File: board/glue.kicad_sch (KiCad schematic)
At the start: 2 parts, among them U9 ATF1504AS-xAx44

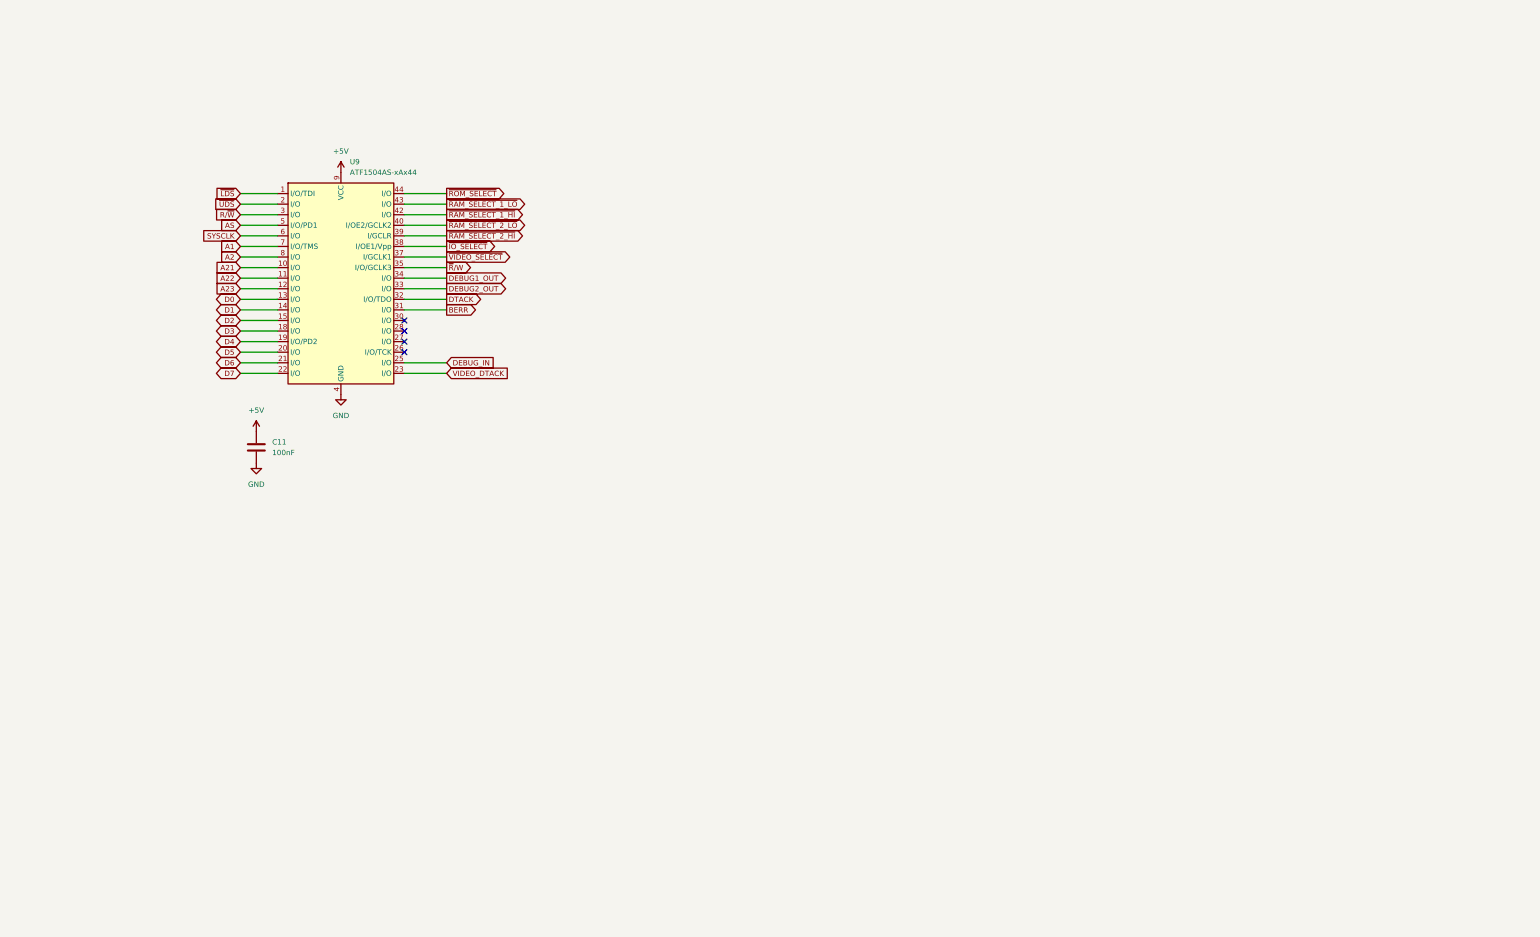
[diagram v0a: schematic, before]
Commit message: fill out most functionality - passes ERC
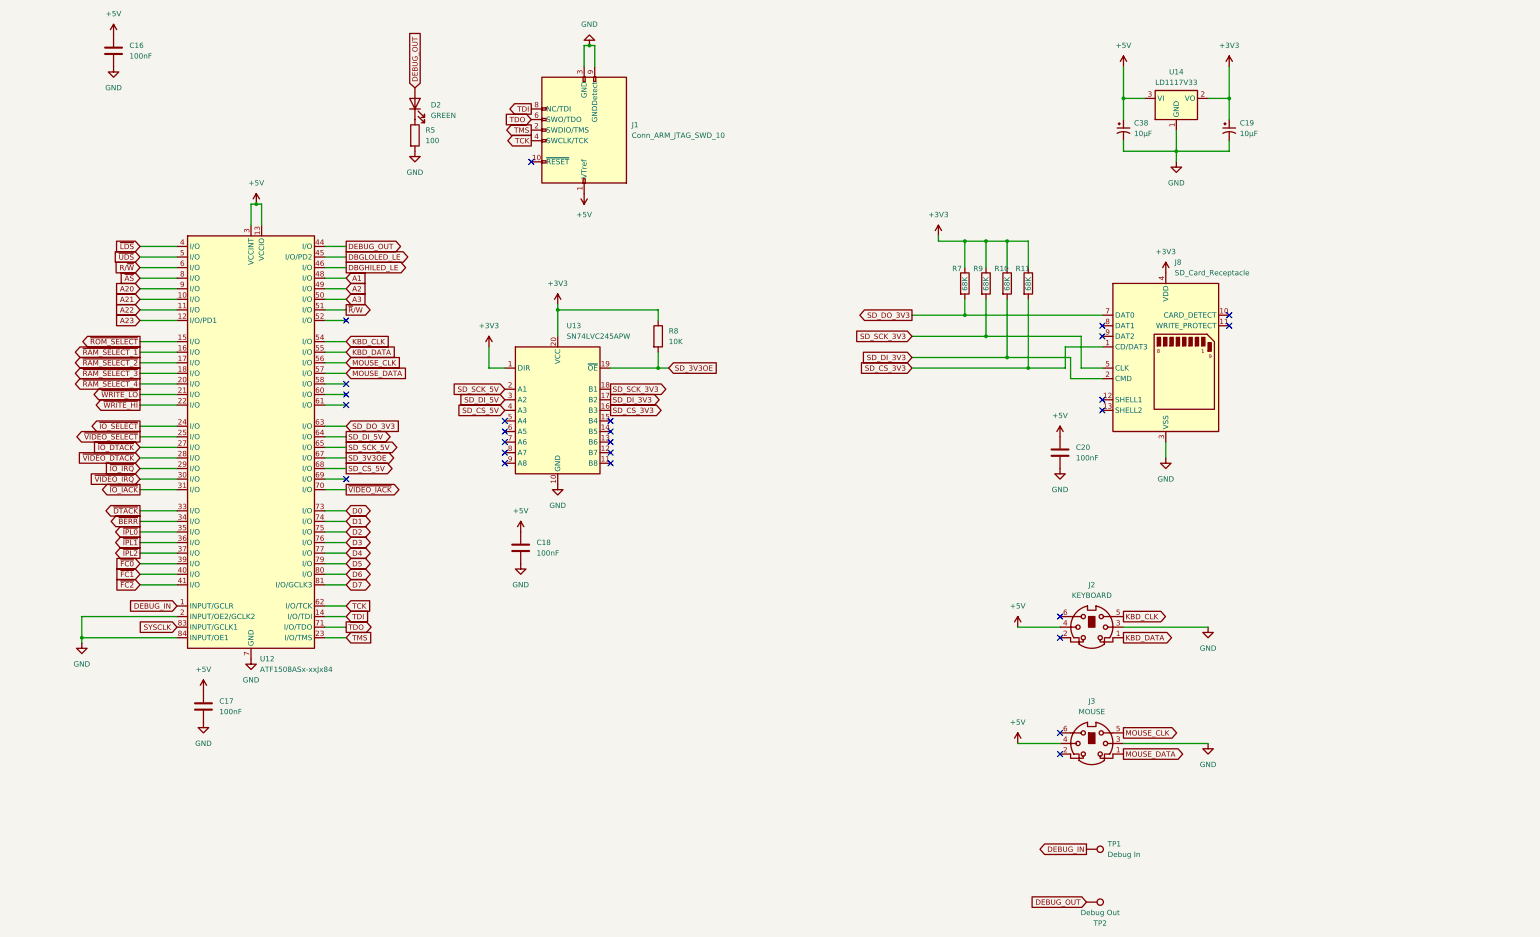
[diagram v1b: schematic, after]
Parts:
- removed U9: ATF1504AS-xAx44, Package_QFP:TQFP-44_10x10mm_P0.8mm, symbol CPLD_Microchip:ATF1504AS-xAx44
- added C16, C18, C20: 100nF, symbol Device:C
- added C19, C38: 10µF, symbol Device:C_Polarized_Small_US
- added D2: GREEN, LED_THT:LED_D3.0mm, symbol Device:LED
- added J1: Conn_ARM_JTAG_SWD_10, symbol Connector:Conn_ARM_JTAG_SWD_10
- added J2: KEYBOARD, symbol Connector:Mini-DIN-6
- added J3: MOUSE, symbol Connector:Mini-DIN-6
- added J8: SD_Card_Receptacle, symbol Connector:SD_Card_Receptacle
- added R10, R11, R7, R9: 68K, symbol Device:R
- added R5: 100, symbol Device:R
- added R8: 10K, symbol Device:R
- added TP1: Debug In, symbol Connector:TestPoint
- added TP2: Debug Out, symbol Connector:TestPoint
- added U12: ATF1508ASx-xxJx84, Package_LCC:PLCC-84_29.3x29.3mm_P1.27mm, symbol CPLD_Microchip:ATF1508ASx-xxJx84
- added U13: SN74LVC245APW, Package_SO:TSSOP-20_4.4x6.5mm_P0.65mm, symbol Logic_LevelTranslator:SN74LVC245APW
- added U14: LD1117V33, Package_TO_SOT_THT:TO-220-3_Vertical, symbol Regulator_Linear:LD1117V33
- renumbered C11 to C17
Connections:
- net +5V: now also C16.1, C18.1, C20.1, C38.1, J1.1 (VTref), J2.4, J3.4, U12.13 (VCCIO), U12.26 (VCCIO), U12.3 (VCCINT), U12.38 (VCCIO), U12.43 (VCCINT), U12.53 (VCCIO), U12.66 (VCCIO), U12.78 (VCCIO), U14.3 (VI)
- net A1: now also U12.48 (I/O)
- net A2: now also U12.49 (I/O)
- net A21: now also U12.10 (I/O)
- net A22: now also U12.11 (I/O)
- net A23: now also U12.12 (I/O/PD1)
- net D0: now also U12.73 (I/O)
- net D1: now also U12.74 (I/O)
- net D2: now also U12.75 (I/O)
- net D3: now also U12.76 (I/O)
- net D4: now also U12.77 (I/O)
- net D5: now also U12.79 (I/O)
- net D6: now also U12.80 (I/O)
- net D7: now also U12.81 (I/O/GCLK3)
- net DEBUG_IN: now also TP1.1, U12.1 (INPUT/GCLR)
- net GND: now also C16.2, C18.2, C19.2, C20.2, C38.2, J1.3 (GND), J1.5 (GND), J1.9 (GNDDetect), J2.3, J3.3, J8.3 (VSS), J8.6 (VSS), R5.2, U12.19 (GND), U12.2 (INPUT/OE2/GCLK2), U12.32 (GND), U12.42 (GND), U12.47 (GND), U12.59 (GND), U12.7 (GND), U12.72 (GND), U12.82 (GND), U12.84 (INPUT/OE1), U13.10 (GND), U14.1 (GND)
- net R/~{W}: now also U12.6 (I/O)
- net SYSCLK: now also U12.83 (INPUT/GCLK1)
- net ~{IO_SELECT}: now also U12.24 (I/O)
- net ~{LDS}: now also U12.4 (I/O)
- net ~{ROM_SELECT}: now also U12.15 (I/O)
- net ~{R}/W: now also U12.51 (I/O)
- net ~{UDS}: now also U12.5 (I/O)
- net ~{VIDEO_SELECT}: now also U12.25 (I/O)
- new net: D2.1 (K), R5.1
- new net +3V3: C19.1, J8.4 (VDD), R10.1, R11.1, R7.1, R8.1, R9.1, U13.1 (DIR), U13.20 (VCC), U14.2 (VO)
- new net A20: U12.9 (I/O)
- new net A3: U12.50 (I/O)
- new net DBGHILED_LE: U12.46 (I/O)
- new net DBGLOLED_LE: U12.45 (I/O/PD2)
- new net DEBUG_OUT: D2.2 (A), TP2.1, U12.44 (I/O)
- new net KBD_CLK: J2.5, U12.54 (I/O)
- new net KBD_DATA: J2.1, U12.55 (I/O)
- new net MOUSE_CLK: J3.5, U12.56 (I/O)
- new net MOUSE_DATA: J3.1, U12.57 (I/O)
- new net SD_3V3OE: R8.2, U12.67 (I/O), U13.19 (~{OE})
- new net SD_CS_3V3: J8.1 (CD/DAT3), R11.2, U13.16 (B3)
- new net SD_CS_5V: U12.68 (I/O), U13.4 (A3)
- new net SD_DI_3V3: J8.2 (CMD), R10.2, U13.17 (B2)
- new net SD_DI_5V: U12.64 (I/O), U13.3 (A2)
- new net SD_DO_3V3: J8.7 (DAT0), R7.2, U12.63 (I/O)
- new net SD_SCK_3V3: J8.5 (CLK), R9.2, U13.18 (B1)
- new net SD_SCK_5V: U12.65 (I/O), U13.2 (A1)
- new net TCK: J1.4 (SWCLK/TCK), U12.62 (I/O/TCK)
- new net TDI: J1.8 (NC/TDI), U12.14 (I/O/TDI)
- new net TDO: J1.6 (SWO/TDO), U12.71 (I/O/TDO)
- new net TMS: J1.2 (SWDIO/TMS), U12.23 (I/O/TMS)
- new net ~{AS}: U12.8 (I/O)
- new net ~{BERR}: U12.34 (I/O)
- new net ~{DTACK}: U12.33 (I/O)
- new net ~{FC0}: U12.39 (I/O)
- new net ~{FC1}: U12.40 (I/O)
- new net ~{FC2}: U12.41 (I/O)
- new net ~{IO_DTACK}: U12.27 (I/O)
- new net ~{IO_IACK}: U12.31 (I/O)
- new net ~{IO_IRQ}: U12.29 (I/O)
- new net ~{IPL0}: U12.35 (I/O)
- new net ~{IPL1}: U12.36 (I/O)
- new net ~{IPL2}: U12.37 (I/O)
- new net ~{RAM_SELECT_1}: U12.16 (I/O)
- new net ~{RAM_SELECT_2}: U12.17 (I/O)
- new net ~{RAM_SELECT_3}: U12.18 (I/O)
- new net ~{RAM_SELECT_4}: U12.20 (I/O)
- new net ~{VIDEO_DTACK}: U12.28 (I/O)
- new net ~{VIDEO_IACK}: U12.70 (I/O)
- new net ~{VIDEO_IRQ}: U12.30 (I/O)
- new net ~{WRITE_HI}: U12.22 (I/O)
- new net ~{WRITE_LO}: U12.21 (I/O)
- no-connect marks 4 -> 26
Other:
- moved on the sheet: C17

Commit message: change IO to 8051 variant, add audio
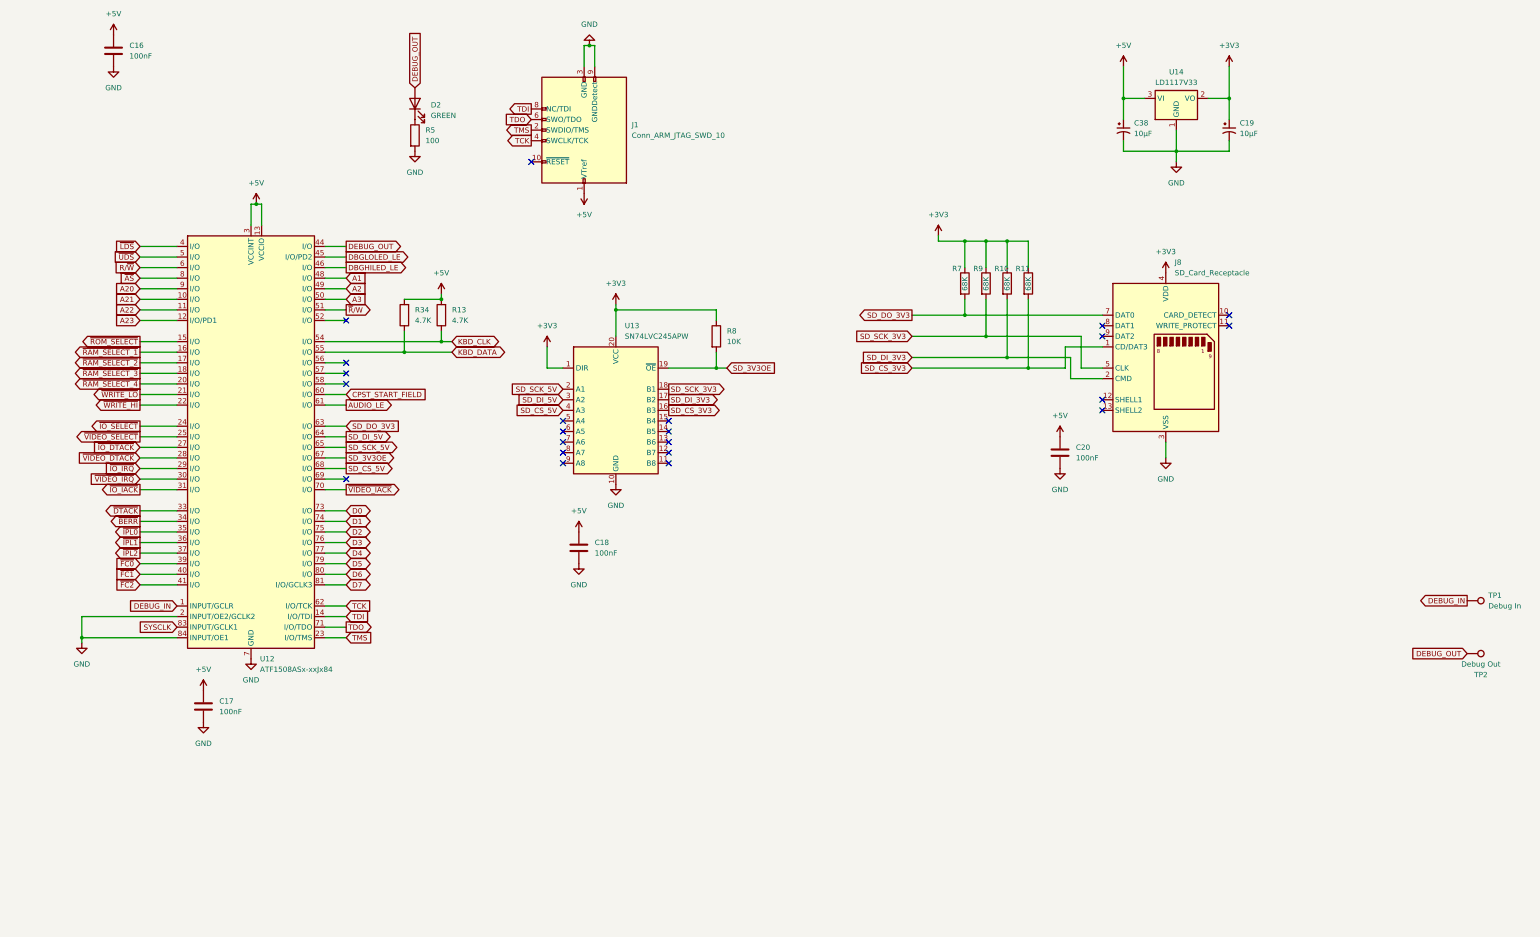
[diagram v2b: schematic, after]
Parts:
- removed J2: KEYBOARD, symbol Connector:Mini-DIN-6
- removed J3: MOUSE, symbol Connector:Mini-DIN-6
- added R13, R34: 4.7K, symbol Device:R
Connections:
- net +5V: now also R13.2, R34.2
- net KBD_CLK: now also R13.1
- net KBD_DATA: now also R34.1
- net CPST_START_FIELD: now reaches U12.60 (I/O)
- net AUDIO_LE: now reaches U12.61 (I/O)
- net MOUSE_CLK: no longer names the net of U12.56 (I/O)
- net MOUSE_DATA: no longer names the net of U12.57 (I/O)
- no-connect marks 26 -> 22
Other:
- moved on the sheet: C18, R8, TP1, TP2, U13

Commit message: design draft complete, added footprints
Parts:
- removed C16: 100nF, symbol Device:C
- removed R13, R34: 4.7K, symbol Device:R
- added R56: 10K, Resistor_THT:R_Axial_DIN0207_L6.3mm_D2.5mm_P10.16mm_Horizontal, symbol Device:R
- C17, C18, C20: footprint (none) -> Capacitor_THT:C_Disc_D5.0mm_W2.5mm_P5.00mm
- C19, C38: footprint (none) -> Capacitor_THT:CP_Radial_D5.0mm_P2.50mm
- J1: footprint (none) -> Connector_PinHeader_1.27mm:PinHeader_2x05_P1.27mm_Vertical
- J8: footprint (none) -> board:10067847-001RLF
- R10, R11, R5, R7, R8, R9: footprint (none) -> Resistor_THT:R_Axial_DIN0207_L6.3mm_D2.5mm_P10.16mm_Horizontal
- TP1, TP2: footprint (none) -> Connector_PinHeader_2.54mm:PinHeader_1x01_P2.54mm_Vertical
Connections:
- net DEBUG_IN: now also R56.1
- net GND: now also R56.2; no longer U12.2 (INPUT/OE2/GCLK2)
- net ~{HALT}: now reaches U12.52 (I/O)
- net KBD_CLK: no longer names the net of U12.54 (I/O)
- net KBD_DATA: no longer names the net of U12.55 (I/O)
- new net ~{RESET}: U12.2 (INPUT/OE2/GCLK2)
- no-connect marks 22 -> 23
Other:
- moved on the sheet: TP1, TP2

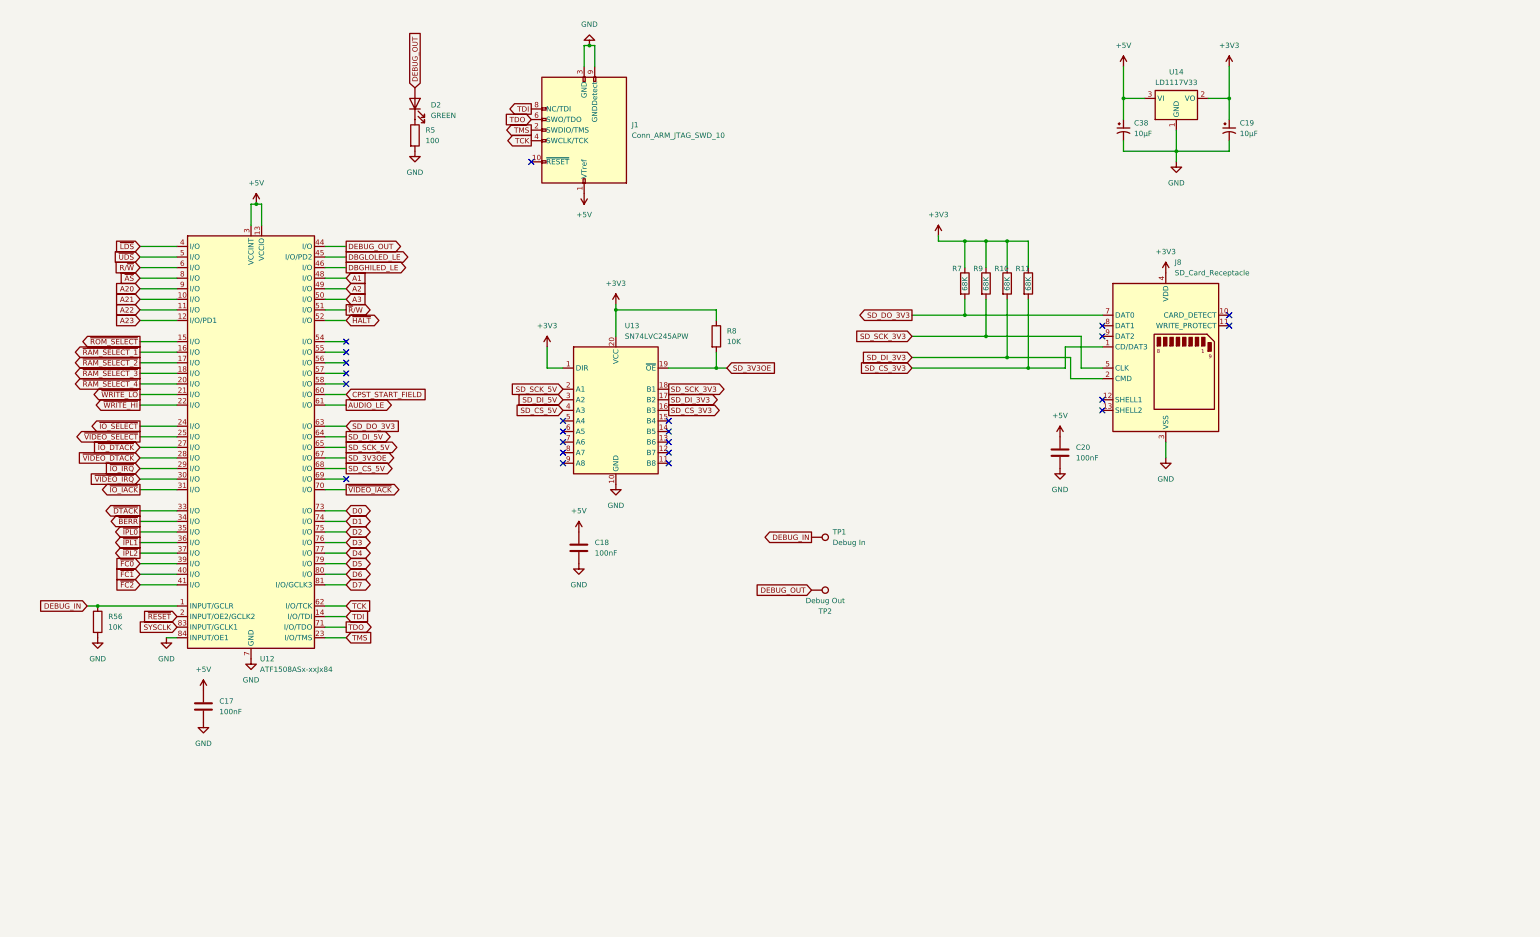
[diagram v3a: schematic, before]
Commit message: start of PCB and MMU
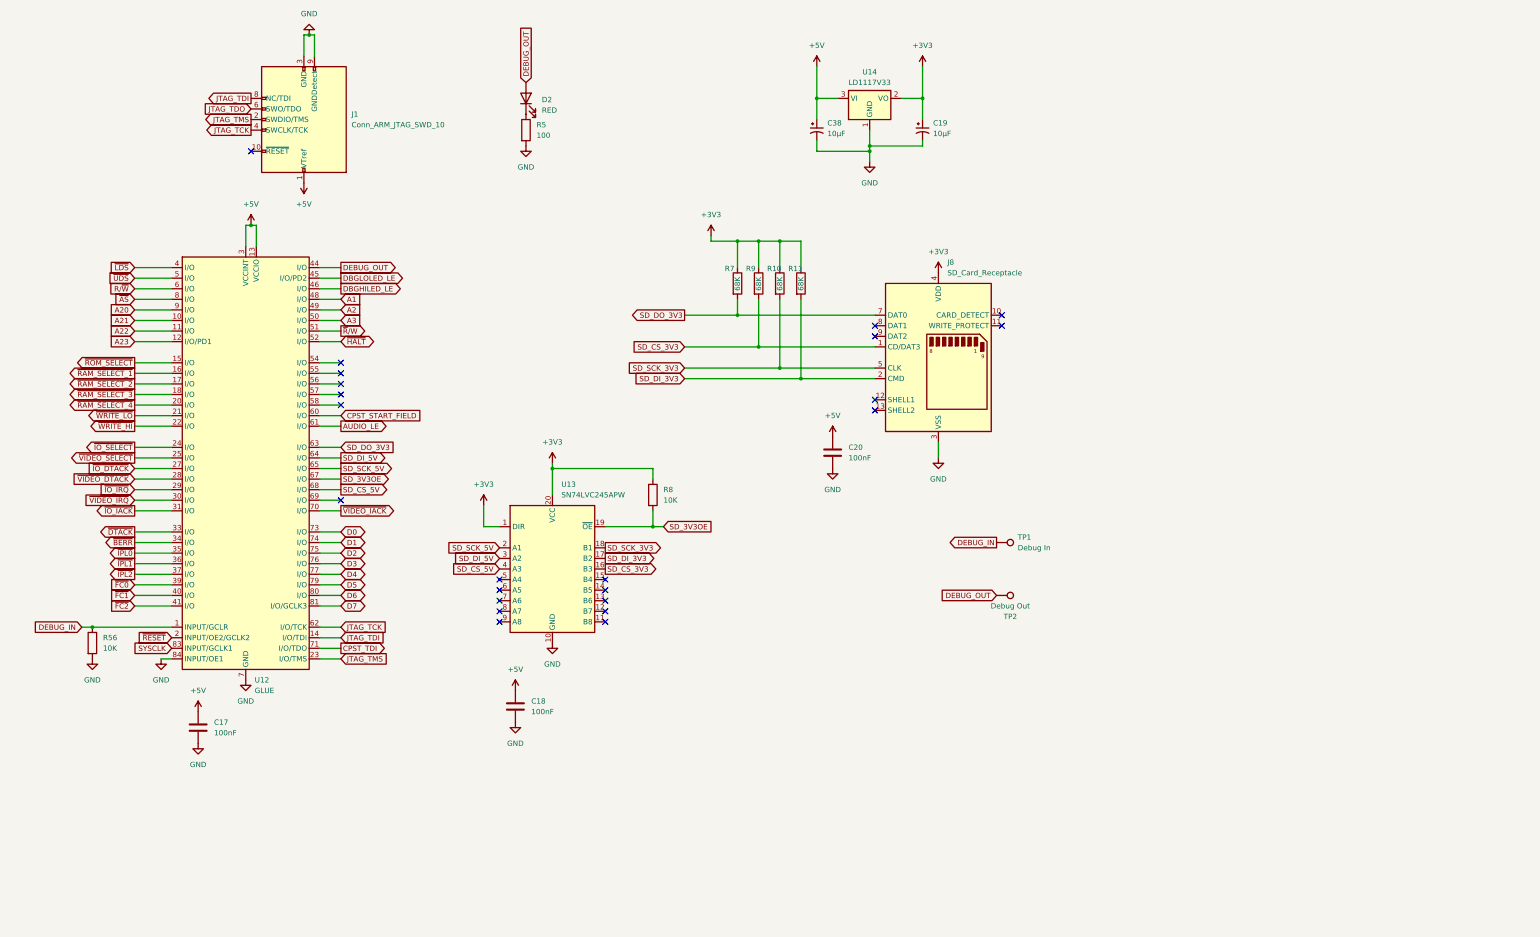
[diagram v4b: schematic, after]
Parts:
- D2: value GREEN -> RED
- U12: value ATF1508ASx-xxJx84 -> GLUE; footprint Package_LCC:PLCC-84_29.3x29.3mm_P1.27mm -> Package_LCC:PLCC-84_THT-Socket
- U13: footprint Package_SO:TSSOP-20_4.4x6.5mm_P0.65mm -> Package_DIP:DIP-20_W7.62mm; Digikey (none) -> https://www.digikey.com/en/products/detail/texas-instrument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
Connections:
- net SD_CS_3V3: now also R9.2; no longer R11.2
- net SD_DI_3V3: now also R11.2; no longer R10.2
- net SD_SCK_3V3: now also R10.2; no longer R9.2
- net TCK renamed JTAG_TCK
- net TDI renamed JTAG_TDI
- net TDO renamed CPST_TDI
- net CPST_TDI: no longer J1.6 (SWO/TDO)
- net TMS renamed JTAG_TMS
- new net JTAG_TDO: J1.6 (SWO/TDO)
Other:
- moved on the sheet: C17, C18, C19, C20, C38, D2, J1, J8, R10, R11, R5, R56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

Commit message: checkpoint
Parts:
- removed J1: Conn_ARM_JTAG_SWD_10, Connector_PinHeader_1.27mm:PinHeader_2x05_P1.27mm_Vertical, symbol Connector:Conn_ARM_JTAG_SWD_10
- added J1: Conn_01x05_Pin, Connector_PinHeader_2.54mm:PinHeader_1x05_P2.54mm_Vertical, symbol Connector:Conn_01x05_Pin
- added LS1: Speaker, Buzzer_Beeper:MagneticBuzzer_StarMicronics_QMX, symbol Device:Speaker
- added R59: 100, Resistor_THT:R_Axial_DIN0207_L6.3mm_D2.5mm_P10.16mm_Horizontal, symbol Device:R
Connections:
- net A1: now also U12.52 (I/O); no longer U12.48 (I/O)
- net A2: now also U12.51 (I/O); no longer U12.49 (I/O)
- net A3: now also U12.54 (I/O); no longer U12.50 (I/O)
- net CPST_START_FIELD: now also U12.69 (I/O); no longer U12.60 (I/O)
- net GND: now also J8.12 (SHELL1), J8.13 (SHELL2), U13.5 (A4), U13.6 (A5), U13.7 (A6), U13.8 (A7), U13.9 (A8), J1.1 (Pin_1), LS1.2; no longer U12.84 (INPUT/OE1)
- net JTAG_TCK: now also J1.2 (Pin_2)
- net JTAG_TDI: now also J1.3 (Pin_3)
- net JTAG_TDO: now also J1.4 (Pin_4)
- net JTAG_TMS: now also J1.5 (Pin_5)
- net ~{HALT}: now also U12.50 (I/O); no longer U12.52 (I/O)
- net ~{R}/W: now also U12.49 (I/O); no longer U12.51 (I/O)
- net A15: now reaches U12.55 (I/O)
- net A16: now reaches U12.56 (I/O)
- net A17: now reaches U12.57 (I/O)
- net A18: now reaches U12.58 (I/O)
- net AUDIO_LE renamed CPST_SELECT
- new net: LS1.1, R59.1
- new net A19: U12.60 (I/O)
- new net BOOT_BEEP: R59.2, U12.48 (I/O)
- new net ~{CPST_DTACK}: U12.84 (INPUT/OE1)
- no-connect marks 23 -> 9
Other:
- note added: "This matches the GND, D0-D3 pins on the Adafruit FT232H breakout"
- moved on the sheet: C20, R10, R11, R7, R9
